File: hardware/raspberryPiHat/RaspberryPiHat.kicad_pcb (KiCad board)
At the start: 2 copper layers, 54.2 x 29.2 mm, 12 parts, among them J1 Raspberry_Pi_2_3, J2 Conn_01x04_Socket, J3 Conn_01x02_Pin, SW1 SW_Push, U1 ESP32-WROOM-32U

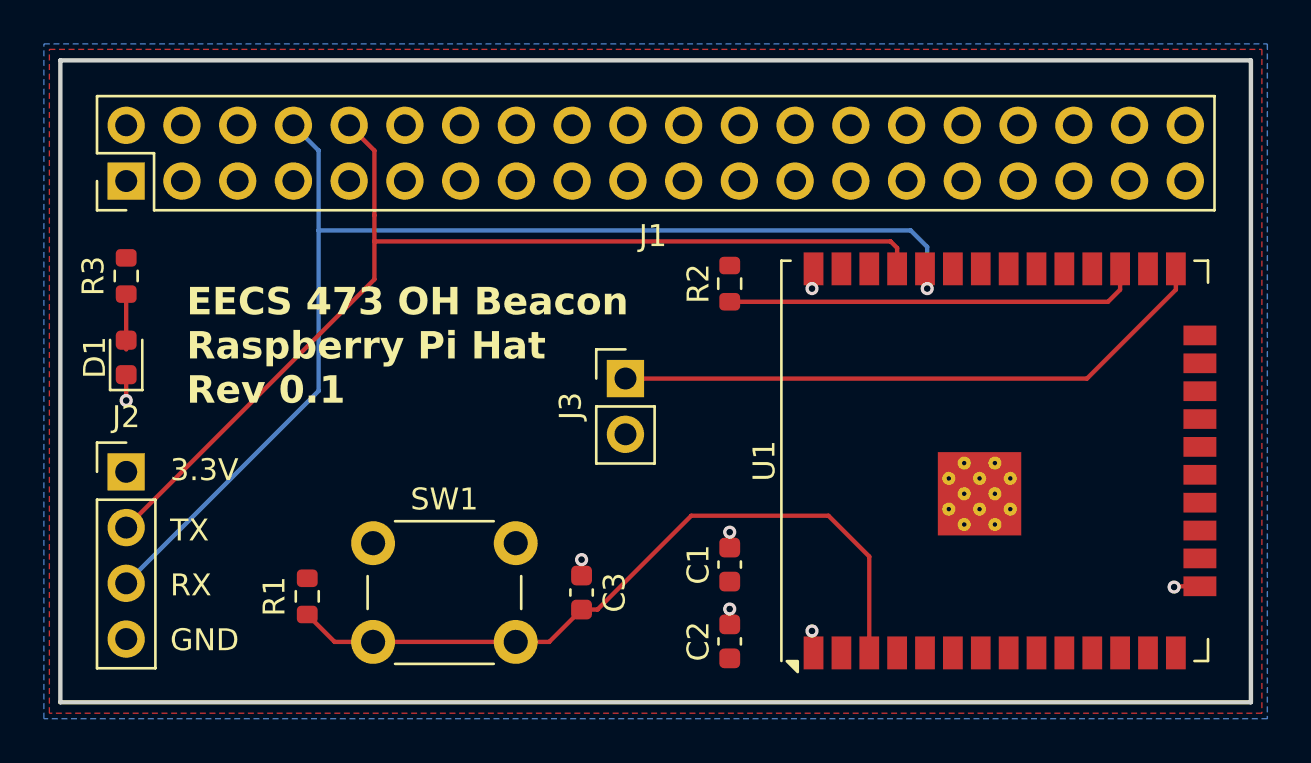
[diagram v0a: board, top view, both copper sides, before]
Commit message: updated rpi
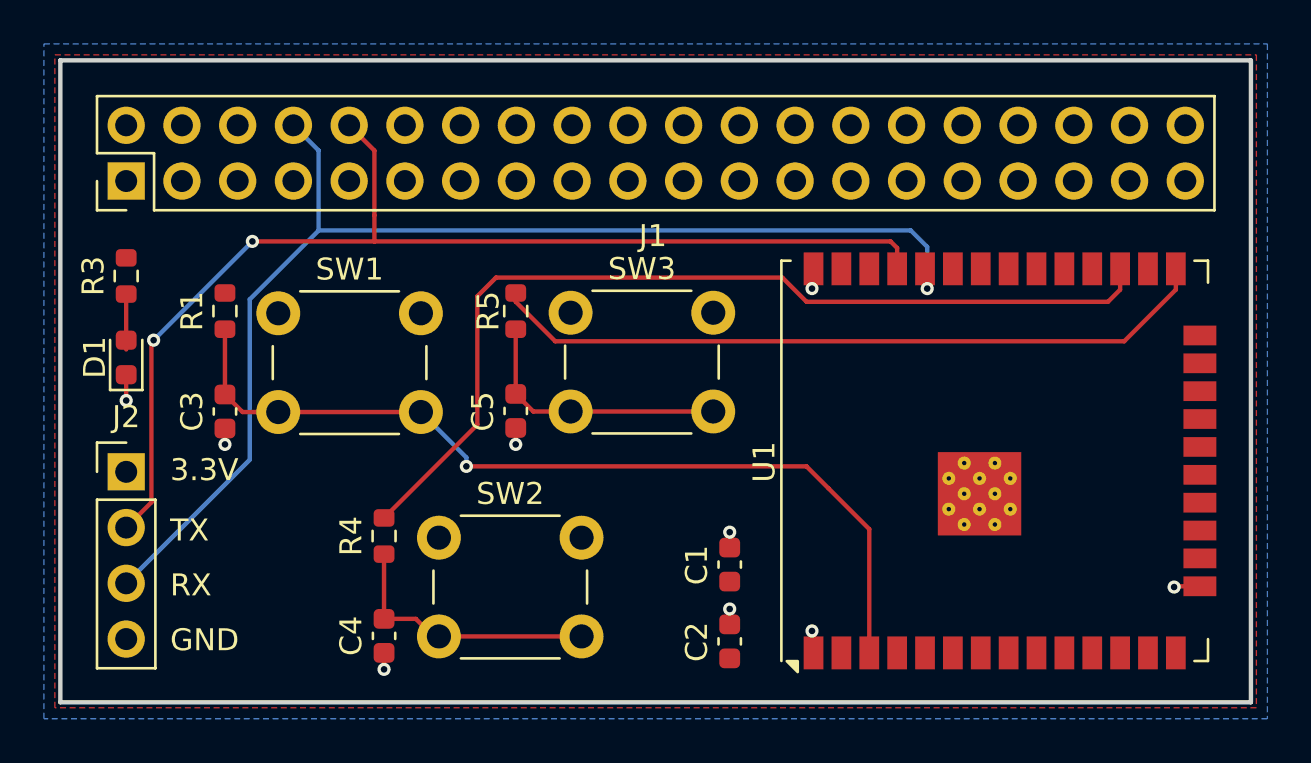
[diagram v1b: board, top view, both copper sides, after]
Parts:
- removed J3: Conn_01x02_Pin, Connector_PinHeader_2.54mm:PinHeader_1x02_P2.54mm_Vertical
- removed R2: 10k, Resistor_SMD:R_0603_1608Metric
- added C4: 0.1uF, Capacitor_SMD:C_0603_1608Metric, F.Cu at (159.8, 113.0)
- added C5: 0.1uF, Capacitor_SMD:C_0603_1608Metric, F.Cu at (165.8, 102.7)
- added R4: 10k, Resistor_SMD:R_0603_1608Metric, F.Cu at (159.8, 108.4)
- added R5: 10k, Resistor_SMD:R_0603_1608Metric, F.Cu at (165.8, 98.2)
- added SW2: SW_Push, Button_Switch_THT:SW_PUSH_6mm, F.Cu at (162.2, 108.5)
- added SW3: SW_Push, Button_Switch_THT:SW_PUSH_6mm, F.Cu at (168.2, 98.2)
- SW1: footprint Buttons_Switches_THT.pretty-master:SW_PUSH_6mm -> Button_Switch_THT:SW_PUSH_6mm
- moved C3 18.2 mm to (152.5, 102.8), turned to -90 degrees
- moved R1 13.5 mm to (152.5, 98.2)
- moved SW1 11.3 mm to (154.9, 98.3)
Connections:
- U1 pad 27: Net-(U1-IO16) -> /MODE
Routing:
- net /MODE: track 0.00 -> 43.1 mm
- net Net-(U1-IO16): track 19.0 -> 0.00 mm
- net Net-(C5-Pad1): track 0.00 -> 12.3 mm
- net Net-(C4-Pad1): track 0.00 -> 12.3 mm
- net Net-(U1-EN): track 33.7 -> 40.8 mm, vias 0 -> 1
- net /IO0: track 27.7 -> 33.1 mm
- net /TXD0: track 48.4 -> 51.9 mm, vias 0 -> 2
- net GND: track 6.02 -> 7.52 mm, vias 7 -> 9
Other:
- board text removed: "EECS 473 OH Beacon Raspberry Pi Hat Rev 0.1"
